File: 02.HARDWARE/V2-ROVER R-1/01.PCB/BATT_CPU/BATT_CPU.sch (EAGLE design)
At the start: 86 parts, among them J1 DF40C_2.0_-20DS-0.4V_51_, J3 N.C, Q1 BSS84W-7-F, Q2 BSS84W-7-F, Q3 2N7002PW, Q4 2N7002PW, Q5 BSS84W-7-F, U1 ATSAMD21G18_QFN, U2 MIC803-26D3VC3-TR, U3 TPS78230DDCR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

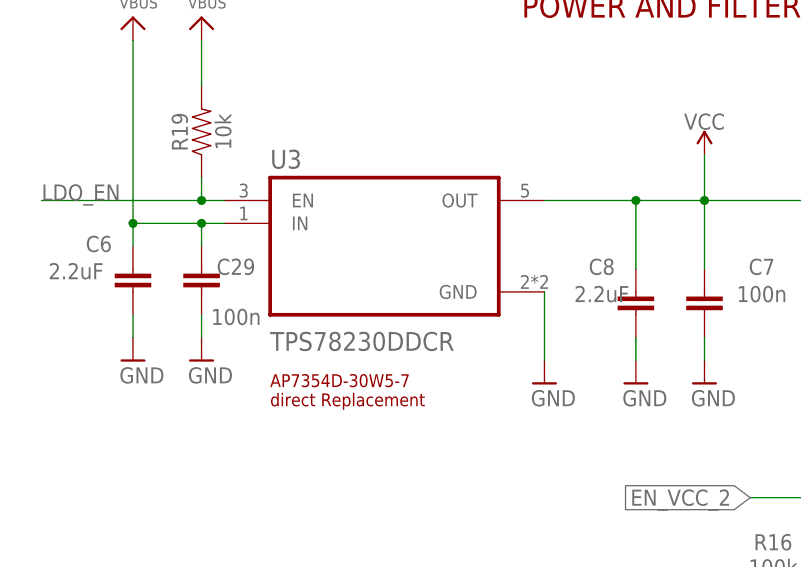
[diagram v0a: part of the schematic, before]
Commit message: Correccion condensadores del LDO de entrada a 10uF. C6 y C8
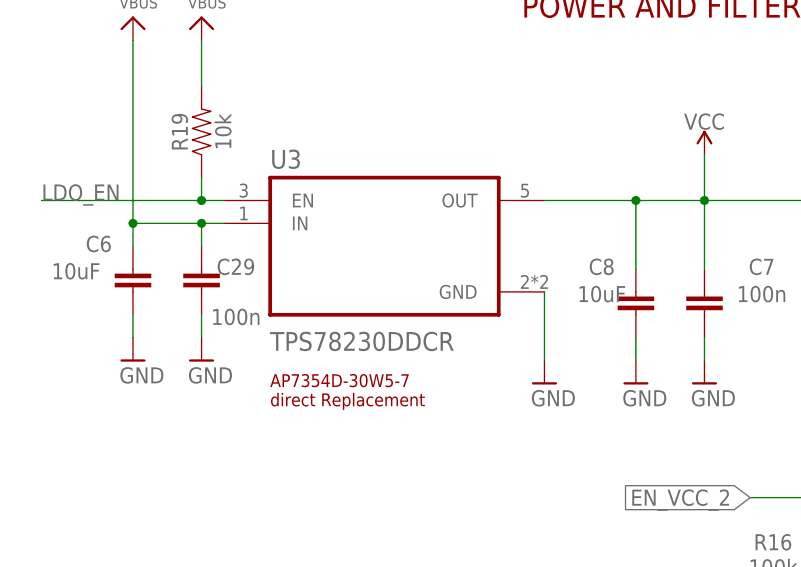
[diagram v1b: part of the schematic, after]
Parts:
- C6, C8: value 2.2uF -> 10uF
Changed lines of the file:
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@@
 </classes>
 <parts>
-<part name="C6" library="SparkFun-Capacitors" library_urn="urn:adsk.eagle:library:510" deviceset="2.2UF" device="-0603-10V-20%" package3d_urn="urn:adsk.eagle:package:37414/1" value="2.2uF"/>
+<part name="C6" library="SparkFun-Capacitors" library_urn="urn:adsk.eagle:library:510" deviceset="2.2UF" device="-0603-10V-20%" package3d_urn="urn:adsk.eagle:package:37414/1" value="10uF"/>
 <part name="U$27" library="microbuilder" deviceset="GND" device=""/>
 <part name="U$28" library="microbuilder" deviceset="GND" device=""/>
-<part name="C8" library="SparkFun-Capacitors" library_urn="urn:adsk.eagle:library:510" deviceset="2.2UF" device="-0603-10V-20%" package3d_urn="urn:adsk.eagle:package:37414/1" value="2.2uF"/>
+<part name="C8" library="SparkFun-Capacitors" library_urn="urn:adsk.eagle:library:510" deviceset="2.2UF" device="-0603-10V-20%" package3d_urn="urn:adsk.eagle:package:37414/1" value="10uF"/>
 <part name="U$29" library="microbuilder" deviceset="GND" device=""/>
 <part name="GND12" library="supply1" deviceset="GND" device=""/>

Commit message: Issue #72
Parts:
- R18: value 100k -> 10k
- R48: value 10k -> 1k
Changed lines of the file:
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@@
 <part name="U$30" library="OLED 66 64x48" deviceset="64X32_OLED_049" device=""/>
 <part name="C19" library="SparkFun-Capacitors" library_urn="urn:adsk.eagle:library:510" deviceset="0.1UF" device="-0402-16V-10%" package3d_urn="urn:adsk.eagle:package:37413/1" value="100n"/>
-<part name="R48" library="SparkFun-Resistors" library_urn="urn:adsk.eagle:library:532" deviceset="RESISTOR" device="0402" package3d_urn="urn:adsk.eagle:package:39657/1" value="10k"/>
+<part name="R48" library="SparkFun-Resistors" library_urn="urn:adsk.eagle:library:532" deviceset="RESISTOR" device="0402" package3d_urn="urn:adsk.eagle:package:39657/1" value="1k"/>
 <part name="Q1" library="BSS84W-7-F" deviceset="BSS84W-7-F" device=""/>
 <part name="R5" library="SparkFun-Resistors" library_urn="urn:adsk.eagle:library:532" deviceset="RESISTOR" device="0402" package3d_urn="urn:adsk.eagle:package:39657/1" value="47k"/>
@@
 <part name="SUPPLY11" library="SparkFun-PowerSymbols" deviceset="VCC" device="" value="VCC_2"/>
 <part name="Q5" library="BSS84W-7-F" deviceset="BSS84W-7-F" device=""/>
-<part name="R18" library="SparkFun-Resistors" library_urn="urn:adsk.eagle:library:532" deviceset="RESISTOR" device="0402" package3d_urn="urn:adsk.eagle:package:39657/1" value="100k"/>
+<part name="R18" library="SparkFun-Resistors" library_urn="urn:adsk.eagle:library:532" deviceset="RESISTOR" device="0402" package3d_urn="urn:adsk.eagle:package:39657/1" value="10k"/>
 <part name="U$31" library="microbuilder" deviceset="GND" device=""/>
 <part name="C27" library="SparkFun-Capacitors" library_urn="urn:adsk.eagle:library:510" deviceset="0.1UF" device="-0402-16V-10%" package3d_urn="urn:adsk.eagle:package:37413/1" value="100n"/>

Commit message: Issue #73
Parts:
- removed J3: N.C, SparkFun-Jumpers:JUMPER-SMT_2_NC_PASTE_SILK
- removed U2: MIC803-26D3VC3-TR, MIC803-26D3VC3-TR:MIC803-26D3VC3-TR
- added R22: 7k5, SparkFun-Resistors:RESISTOR0402
- R18: value 10k -> 100k
- R48: value 1k -> 10k
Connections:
- net !RESET: no longer J3.1, U2.!RESET
- net GND: now also R22.1; no longer U2.GND
- net LDO_EN: now also R22.2; no longer J3.2
- net VBUS: no longer U2.VCC
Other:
- moved on the sheet: C29, C6, C7, C8, R19, R5, U3
